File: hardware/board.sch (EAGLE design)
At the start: 47 parts, among them IC1 0915BM15A0001, J1 U.FL, U2 TPS63030DSKT, U3 BLE113-A, X1 CTS_32X25_SMD, X3 MINI-USB-UX60-MB-5ST

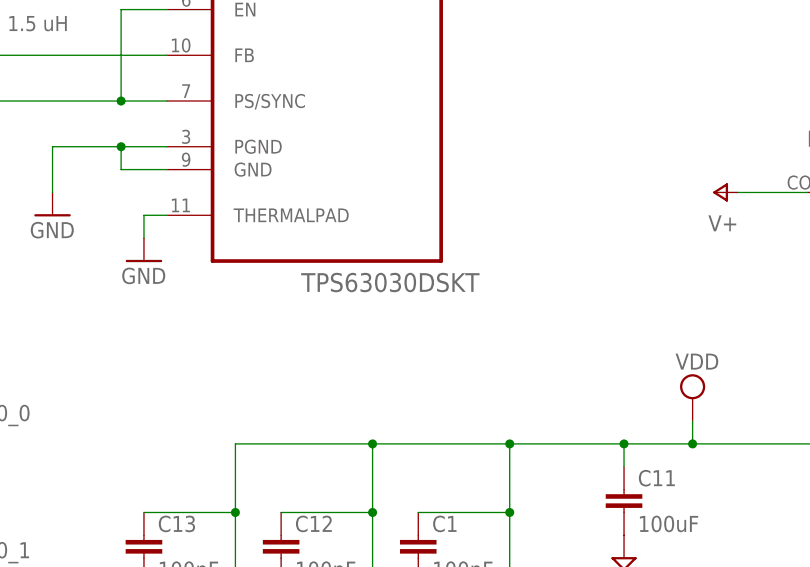
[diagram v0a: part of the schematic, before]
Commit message: Fix coverter part number
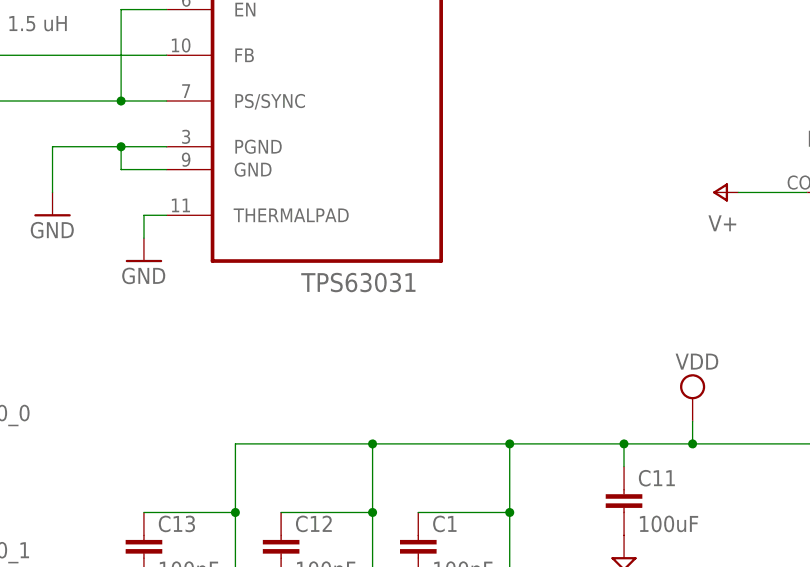
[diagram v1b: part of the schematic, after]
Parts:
- U2: value TPS63030DSKT -> TPS63031; device Texas Instruments_By_element14_Batch_1:TPS63030DSKT -> Texas Instruments_By_element14_Batch_1:TPS63031; MPN (none) -> TPS63031
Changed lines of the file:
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@@
 <part name="GND5" library="supply1" deviceset="GND" device=""/>
 <part name="GND6" library="supply1" deviceset="GND" device=""/>
-<part name="U2" library="Texas Instruments_By_element14_Batch_1" deviceset="TPS63030DSKT" device=""/>
+<part name="U2" library="Texas Instruments_By_element14_Batch_1" deviceset="TPS63031" device="">
+<attribute name="MPN" value="TPS63031"/>
+</part>
 <part name="GND7" library="supply1" deviceset="GND" device=""/>
 <part name="GND8" library="supply1" deviceset="GND" device=""/>

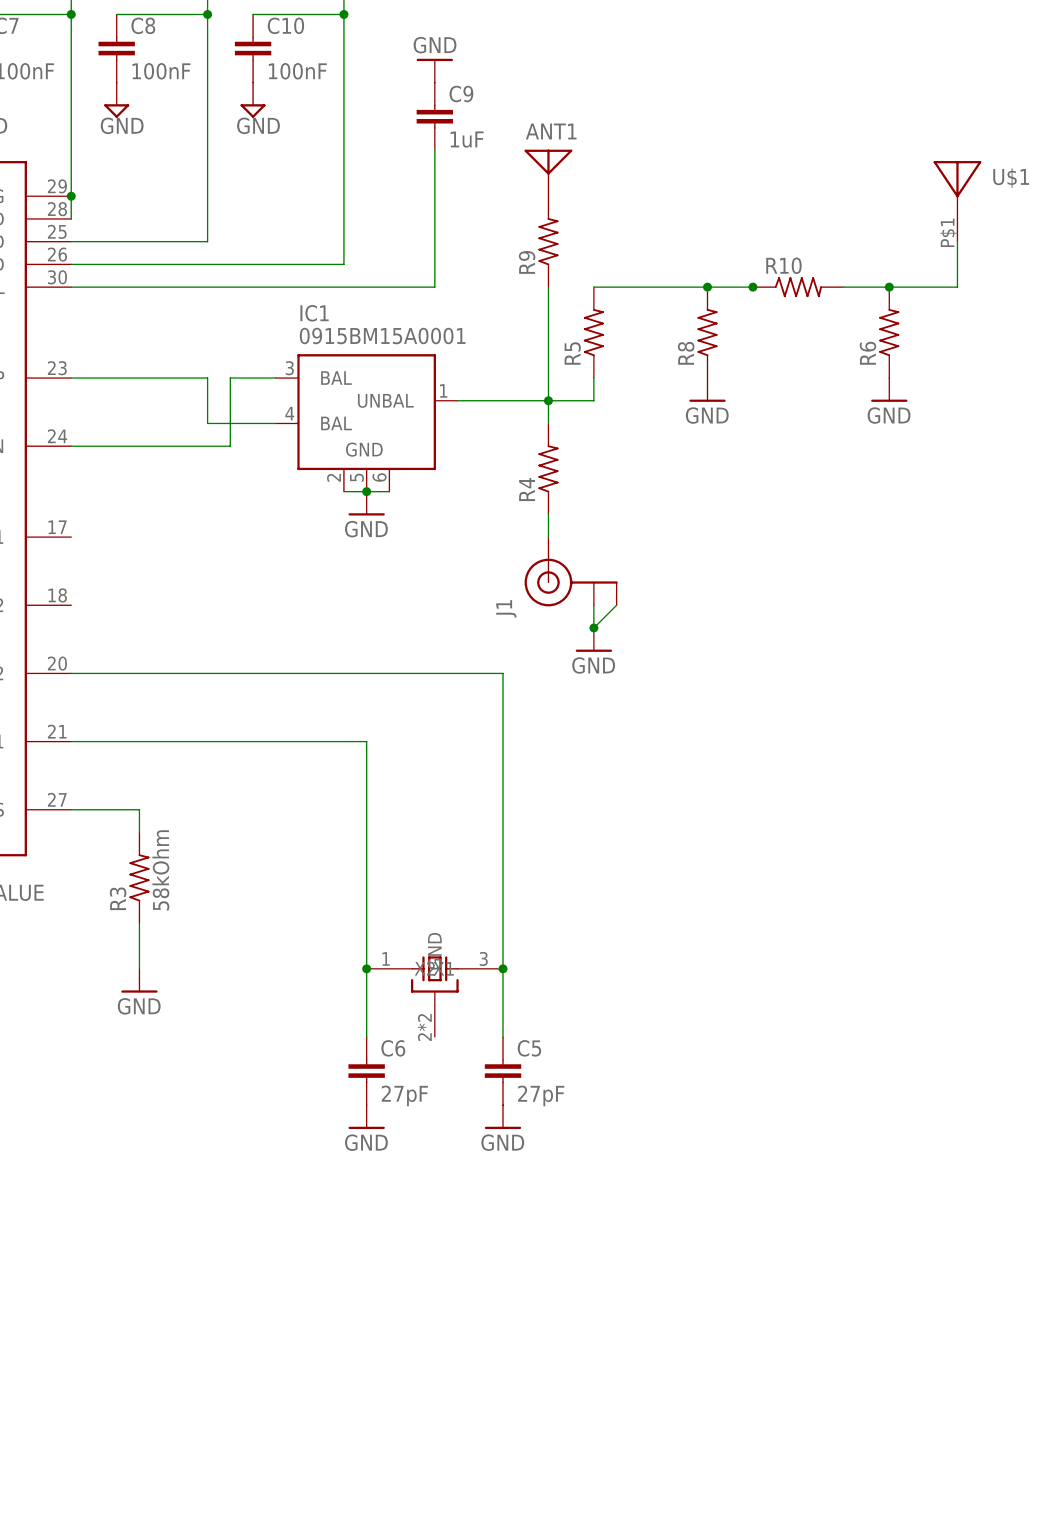
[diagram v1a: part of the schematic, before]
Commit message: Remove chip antenna, add fiducials, clean up labels, annotate RileyLink0.3
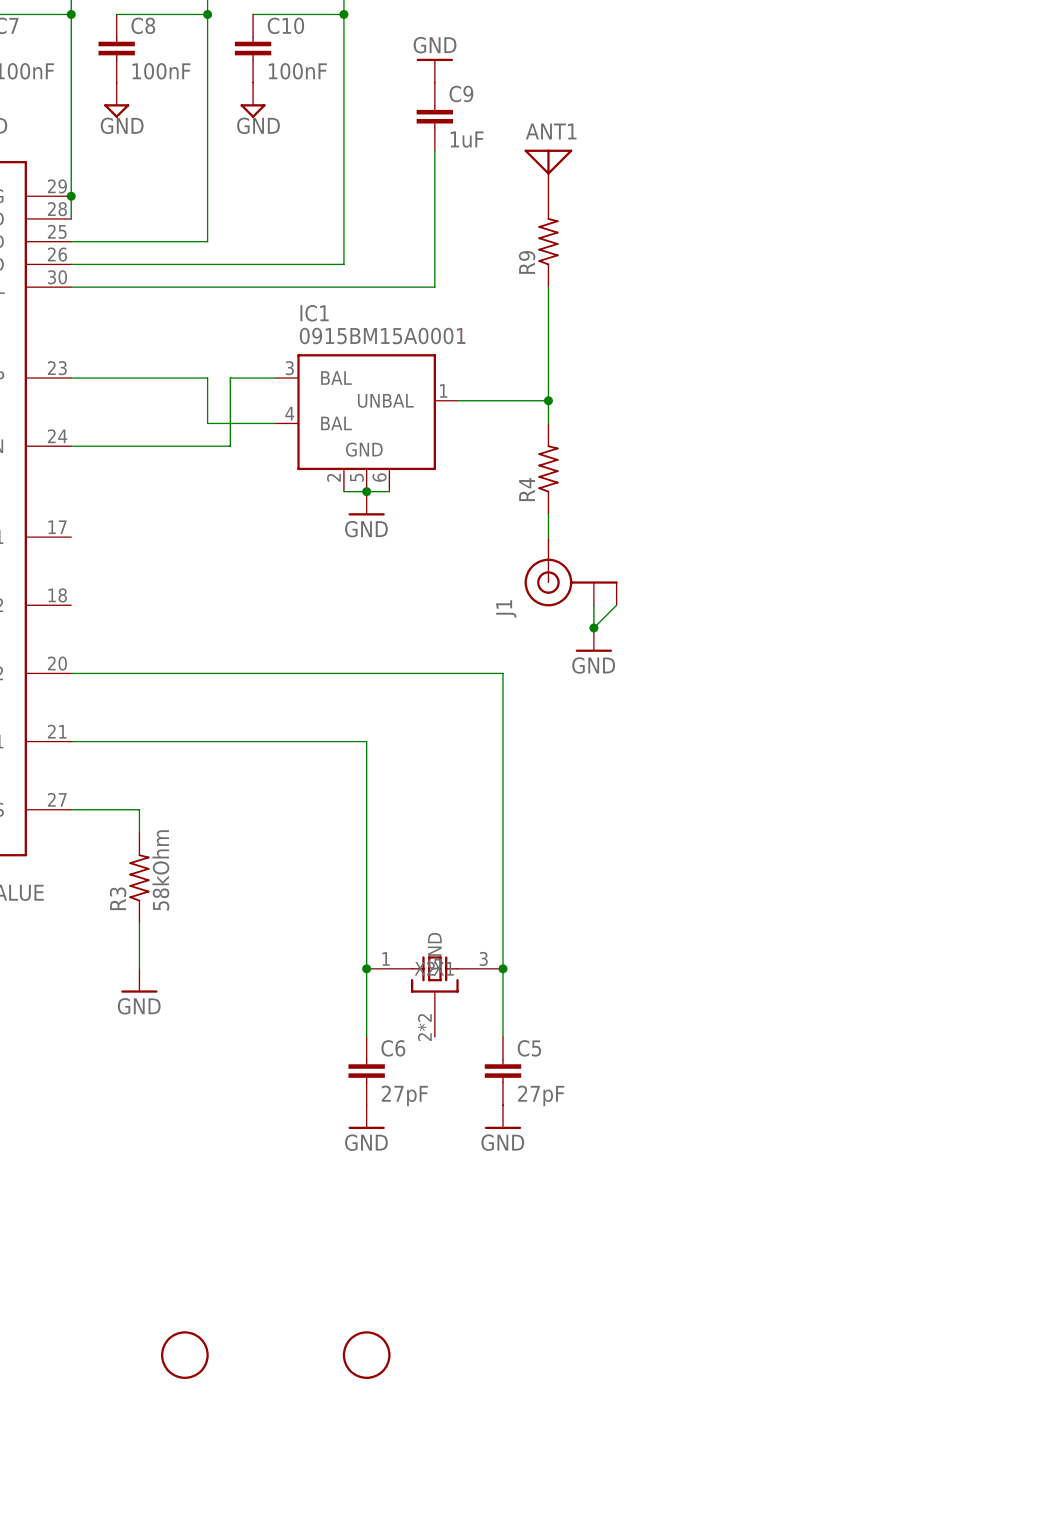
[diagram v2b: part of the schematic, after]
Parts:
- removed R10, R5, R6, R8: (no value), rcl:R-US_R0402
- added U$3: FIDUCIAL, adafruit:FIDUCIAL
- U$1: value 915_ANT -> FIDUCIAL; device parts:915_ANT -> adafruit:FIDUCIAL
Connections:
- removed net N$11: R10.1, R5.2, R8.2
- removed net N$13: R10.2, R6.2, U$1.P$1
- net GND: no longer R6.1, R8.1
- net N$10: no longer R5.1
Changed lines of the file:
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@@
 <layer number="113" name="IDFDebug" color="4" fill="1" visible="yes" active="yes"/>
 <layer number="116" name="Patch_BOT" color="9" fill="4" visible="yes" active="yes"/>
+<layer number="118" name="Rect_Pads" color="7" fill="1" visible="no" active="no"/>
 <layer number="121" name="_tsilk" color="7" fill="1" visible="yes" active="yes"/>
 <layer number="122" name="_bsilk" color="7" fill="1" visible="yes" active="yes"/>
@@
 <part name="GND10" library="supply1" deviceset="GND" device=""/>
 <part name="R4" library="rcl" deviceset="R-US_" device="R0402"/>
-<part name="R5" library="rcl" deviceset="R-US_" device="R0402"/>
-<part name="R6" library="rcl" deviceset="R-US_" device="R0402"/>
-<part name="R8" library="rcl" deviceset="R-US_" device="R0402"/>
 <part name="ANT1" library="discrete" deviceset="ANTENNA" device=""/>
 <part name="R9" library="rcl" deviceset="R-US_" device="R0402"/>
-<part name="R10" library="rcl" deviceset="R-US_" device="R0402"/>
-<part name="GND11" library="supply1" deviceset="GND" device=""/>
-<part name="GND12" library="supply1" deviceset="GND" device=""/>
-<part name="U$1" library="parts" deviceset="915_ANT" device=""/>
 <part name="CC1110-DEBUG" library="parts" deviceset="CC-DEBUG-PWR" device=""/>
 <part name="BLE113-DEBUG" library="parts" deviceset="CC-DEBUG-PWR" device=""/>
@@
 <part name="SUPPLY18" library="supply2" deviceset="VDD" device=""/>
 <part name="GND20" library="supply1" deviceset="GND" device=""/>
+<part name="U$1" library="adafruit" deviceset="FIDUCIAL" device=""/>
+<part name="U$3" library="adafruit" deviceset="FIDUCIAL" device=""/>
 </parts>
 <sheets>
@@
 <instance part="GND10" gate="1" x="132.08" y="43.18"/>
 <instance part="R4" gate="G$1" x="152.4" y="48.26" rot="R90"/>
-<instance part="R5" gate="G$1" x="157.48" y="63.5" rot="R90"/>
-<instance part="R6" gate="G$1" x="190.5" y="63.5" rot="R90"/>
-<instance part="R8" gate="G$1" x="170.18" y="63.5" rot="R90"/>
 <instance part="ANT1" gate="A" x="152.4" y="83.82"/>
 <instance part="R9" gate="G$1" x="152.4" y="73.66" rot="R90"/>
-<instance part="R10" gate="G$1" x="180.34" y="68.58"/>
-<instance part="GND11" gate="1" x="170.18" y="55.88"/>
-<instance part="GND12" gate="1" x="190.5" y="55.88"/>
-<instance part="U$1" gate="G$1" x="198.12" y="78.74"/>
 <instance part="CC1110-DEBUG" gate="G$1" x="-17.78" y="55.88" rot="R180"/>
 <instance part="BLE113-DEBUG" gate="G$1" x="-15.24" y="-15.24" rot="R180"/>
@@
 <instance part="SUPPLY18" gate="G$1" x="22.86" y="-68.58" rot="R180"/>
 <instance part="GND20" gate="1" x="157.48" y="27.94"/>
+<instance part="U$1" gate="G$1" x="111.76" y="-50.8"/>
+<instance part="U$3" gate="G$1" x="132.08" y="-50.8"/>
 </instances>
 <busses>
@@
 <junction x="132.08" y="45.72"/>
 <pinref part="IC1" gate="G$1" pin="GND@2"/>
-</segment>
-<segment>
-<pinref part="R8" gate="G$1" pin="1"/>
-<pinref part="GND11" gate="1" pin="GND"/>
-</segment>
-<segment>
-<pinref part="R6" gate="G$1" pin="1"/>
-<pinref part="GND12" gate="1" pin="GND"/>
 </segment>
 <segment>
@@
 <pinref part="IC1" gate="G$1" pin="UNBAL"/>
 <wire x1="142.24" y1="55.88" x2="152.4" y2="55.88" width="0.1524" layer="91"/>
-<pinref part="R5" gate="G$1" pin="1"/>
-<wire x1="152.4" y1="55.88" x2="157.48" y2="55.88" width="0.1524" layer="91"/>
-<wire x1="157.48" y1="55.88" x2="157.48" y2="58.42" width="0.1524" layer="91"/>
 <junction x="152.4" y="55.88"/>
 <pinref part="R9" gate="G$1" pin="1"/>
@@
 </segment>
 </net>
-<net name="N$11" class="0">
-<segment>
-<pinref part="R10" gate="G$1" pin="1"/>
-<junction x="175.26" y="68.58"/>
-<pinref part="R10" gate="G$1" pin="1"/>
-<wire x1="175.26" y1="68.58" x2="170.18" y2="68.58" width="0.1524" layer="91"/>
-<pinref part="R8" gate="G$1" pin="2"/>
-<pinref part="R5" gate="G$1" pin="2"/>
-<wire x1="157.48" y1="68.58" x2="170.18" y2="68.58" width="0.1524" layer="91"/>
-<junction x="170.18" y="68.58"/>
-</segment>
-</net>
 <net name="N$12" class="0">
 <segment>
@@
 </segment>
 </net>
-<net name="N$13" class="0">
-<segment>
-<pinref part="R10" gate="G$1" pin="2"/>
-<pinref part="R6" gate="G$1" pin="2"/>
-<wire x1="190.5" y1="68.58" x2="185.42" y2="68.58" width="0.1524" layer="91"/>
-<pinref part="U$1" gate="G$1" pin="P$1"/>
-<wire x1="190.5" y1="68.58" x2="198.12" y2="68.58" width="0.1524" layer="91"/>
-<wire x1="198.12" y1="68.58" x2="198.12" y2="73.66" width="0.1524" layer="91"/>
-<junction x="190.5" y="68.58"/>
-</segment>
-</net>
